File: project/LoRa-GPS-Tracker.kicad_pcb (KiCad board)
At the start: 2 copper layers, 38.9 x 40 mm, 58 parts, among them IC101 MCP73831-2-OT, IC102 MCP100-300D, IC103 FT230XS, IC104 NCP705MT30TCG, M101 SIM28ML, M102 RAK3172, Q101 BSS123, Q102 TP0610K, Q103 BSH205G2VL, SW102 ON/OFF, X101 DEBUG, X102 Conn_Coaxial, X103 BATTERY, X104 DEBUG

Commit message: - Fix wrong pinout for UART bootloader - Update documentation for bootloader
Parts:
- D101: value D_Zener -> SZMM5Z3V3T1G
- D103: value CLS6B-FKW -> STATUS
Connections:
- JP101 pad 1: /Rx_LOG -> /Rx_PROG
- JP101 pad 3: /Rx_PROG -> /Rx_LOG
- JP102 pad 1: /Tx_LOG -> /Tx_PROG
- JP102 pad 3: /Tx_PROG -> /Tx_LOG
- M102 pad 10: /Tx_PROG -> unconnected-(M102-SDA-Pad10)
- M102 pad 20: Net-(M102-PA9) -> /Rx_PROG
- M102 pad 25: unconnected-(M102-ADC4-Pad25) -> /Tx_PROG
- M102 pad 27: unconnected-(M102-PB12-Pad27) -> Net-(M102-PB12)
- M102 pad 9: /Rx_PROG -> unconnected-(M102-SCL-Pad9)
- R119 pad 1: Net-(M102-PA9) -> Net-(M102-PB12)
- X101 pad A8: unconnected-(X101-SBU1-PadA8) -> (no net)
- X101 pad B8: unconnected-(X101-SBU2-PadB8) -> (no net)
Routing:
- net Net-(M102-PB12): track 0.00 -> 44.2 mm, vias 0 -> 2
- net Net-(M102-PA9): track 43.4 -> 0.00 mm, vias 4 -> 0
- net /Tx_PROG: track 5.97 -> 12.9 mm
- net /Rx_PROG: track 9.58 -> 13.9 mm
- net /Tx_LOG: track 12.0 -> 8.75 mm
- net /Rx_LOG: track 15.7 -> 14.2 mm
- net /Rx: track 26.0 -> 25.1 mm

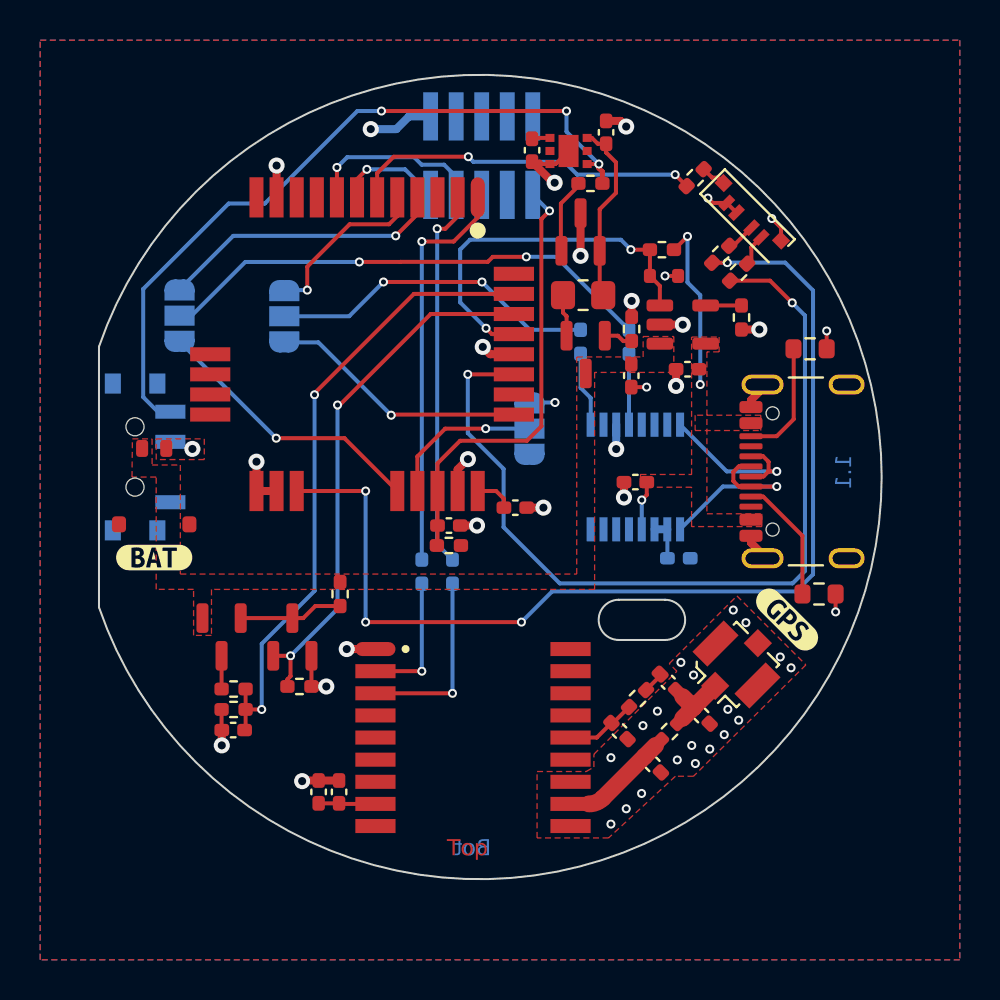
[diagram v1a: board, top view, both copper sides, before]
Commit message: Make it possible to power cycle the GPS module
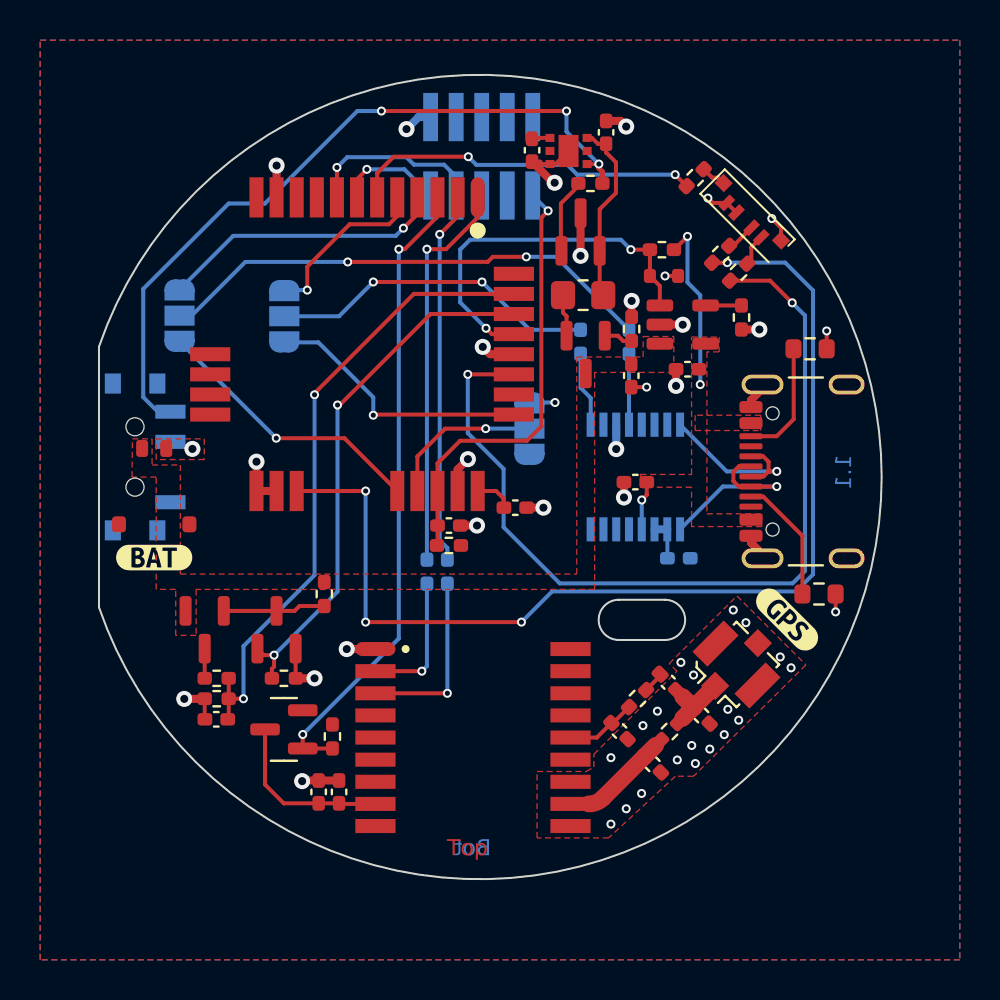
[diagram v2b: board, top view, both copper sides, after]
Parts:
- added Q104: TP0610K, Package_TO_SOT_SMD:SOT-23, F.Cu at (134.7, 118.7)
- added R122: 100k, Resistor_SMD:R_0402_1005Metric_Pad0.72x0.64mm_HandSolder, F.Cu at (137.2, 119.1)
- IC102: value MCP100-300D -> MCP100T-300I/TT
- moved kibuzzard-65A187C4 5.38 mm to (144.6, 94.2), turned to 180 degrees
- moved C103 0.99 mm to (131.4, 118.2)
- moved R105 0.99 mm to (131.4, 116.2)
- moved R106 0.99 mm to (131.4, 117.2)
- moved Q102 0.91 mm to (130.8, 113.8)
- moved R101 0.87 mm to (134.7, 116.2)
- moved Q101 0.86 mm to (134.4, 113.8)
- moved R104 0.79 mm to (136.8, 112.0)
- moved R102 0.25 mm to (141.9, 110.9)
- moved R103 0.25 mm to (142.9, 110.9)
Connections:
- C101 pad 1: +3V0 -> Net-(M101-VCC)
- C102 pad 1: +3V0 -> Net-(M101-VCC)
- M101 pad 8: +3V0 -> Net-(M101-VCC)
- M102 pad 3: unconnected-(M102-ADC5-Pad3) -> /GPS_E
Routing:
- net /GPS_E: track 0.00 -> 31.8 mm, vias 0 -> 2
- net Net-(M101-VCC): track 0.00 -> 8.63 mm
- net +3V0: track 11.4 -> 6.74 mm
- net /Tx_PROG: track 12.9 -> 13.5 mm

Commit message: Add I2C accelerometer
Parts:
- added C112: 100n, Capacitor_SMD:C_0402_1005Metric_Pad0.74x0.62mm_HandSolder, B.Cu at (134.2, 110.8)
- added IC105: LIS2DH, Package_LGA:LGA-14_2x2mm_P0.35mm_LayoutBorder3x4y, B.Cu at (132.3, 109.8)
- added R115: 3k3, Resistor_SMD:R_0402_1005Metric_Pad0.72x0.64mm_HandSolder, B.Cu at (131.3, 106.3)
- added R117: 3k3, Resistor_SMD:R_0402_1005Metric_Pad0.72x0.64mm_HandSolder, B.Cu at (133.2, 107.8)
- renumbered C104 to C103, C105 to C104, C106 to C105, C107 to C106, C108 to C107, C109 to C108, C110 to C109, C111 to C110, C112 to C111, C103 to C115, D103 to D102, Q104 to Q101, Q103 to Q102, Q101 to Q103, Q102 to Q104, R102 to R101, R103 to R102, R122 to R103, R107 to R104, R108 to R105, R109 to R106, R110 to R107, R111 to R108, R112 to R109, R113 to R110, R114 to R111, R115 to R112, R116 to R113, R117 to R114, R118 to R116, R101 to R118, R120 to R119, R119 to R120, R104 to R121, R121 to R122, R105 to R123, R106 to R124, SW102 to SW101
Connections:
- M102 pad 10: unconnected-(M102-SDA-Pad10) -> Net-(IC105-SDA/SDI)
- M102 pad 26: unconnected-(M102-ADC3-Pad26) -> /INT
- M102 pad 9: unconnected-(M102-SCL-Pad9) -> Net-(IC105-SCL/SPC)
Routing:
- net /INT: track 0.00 -> 20.4 mm, vias 0 -> 3
- net Net-(IC105-SCL/SPC): track 0.00 -> 18.7 mm, vias 0 -> 1
- net Net-(IC105-SDA/SDI): track 0.00 -> 18.1 mm, vias 0 -> 1
- net +3V0: track 6.74 -> 11.0 mm, vias 3 -> 7

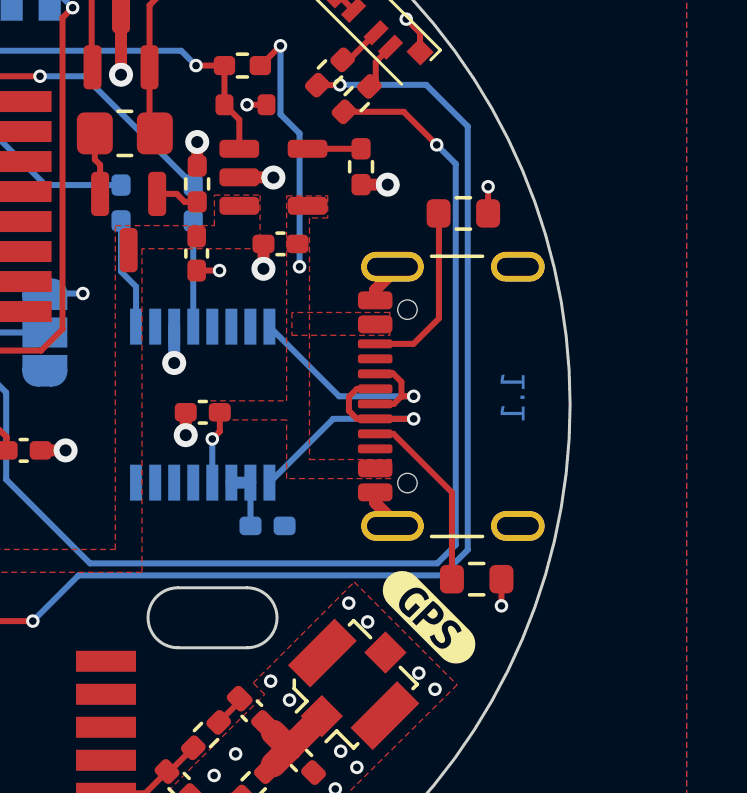
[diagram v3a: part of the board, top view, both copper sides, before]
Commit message: Fix wrong package for CC resistors
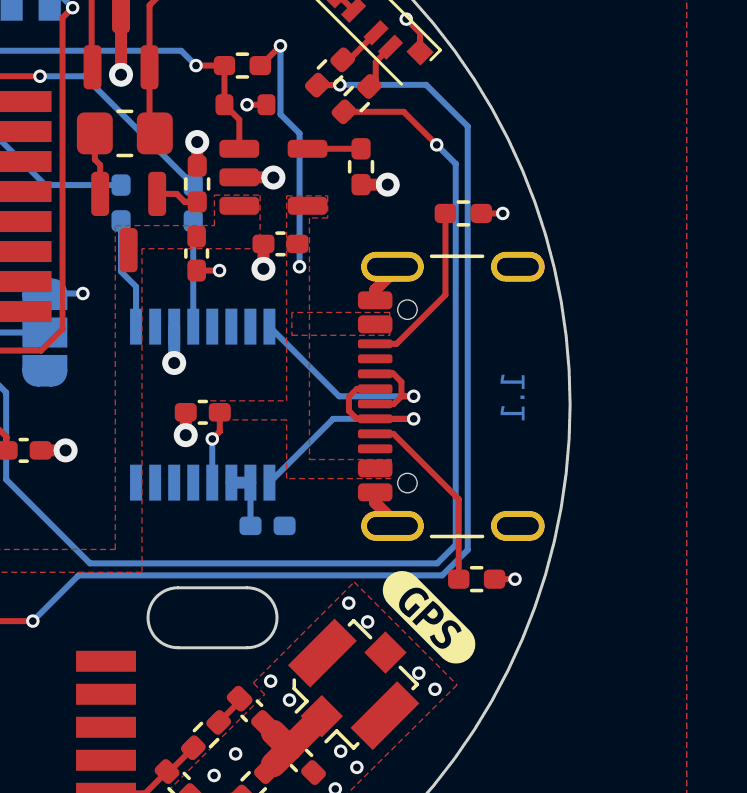
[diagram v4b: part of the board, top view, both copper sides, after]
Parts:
- Q101, Q104: value TP0610K -> BSS84
- R104, R105: footprint Resistor_SMD:R_0603_1608Metric -> Resistor_SMD:R_0402_1005Metric_Pad0.72x0.64mm_HandSolder

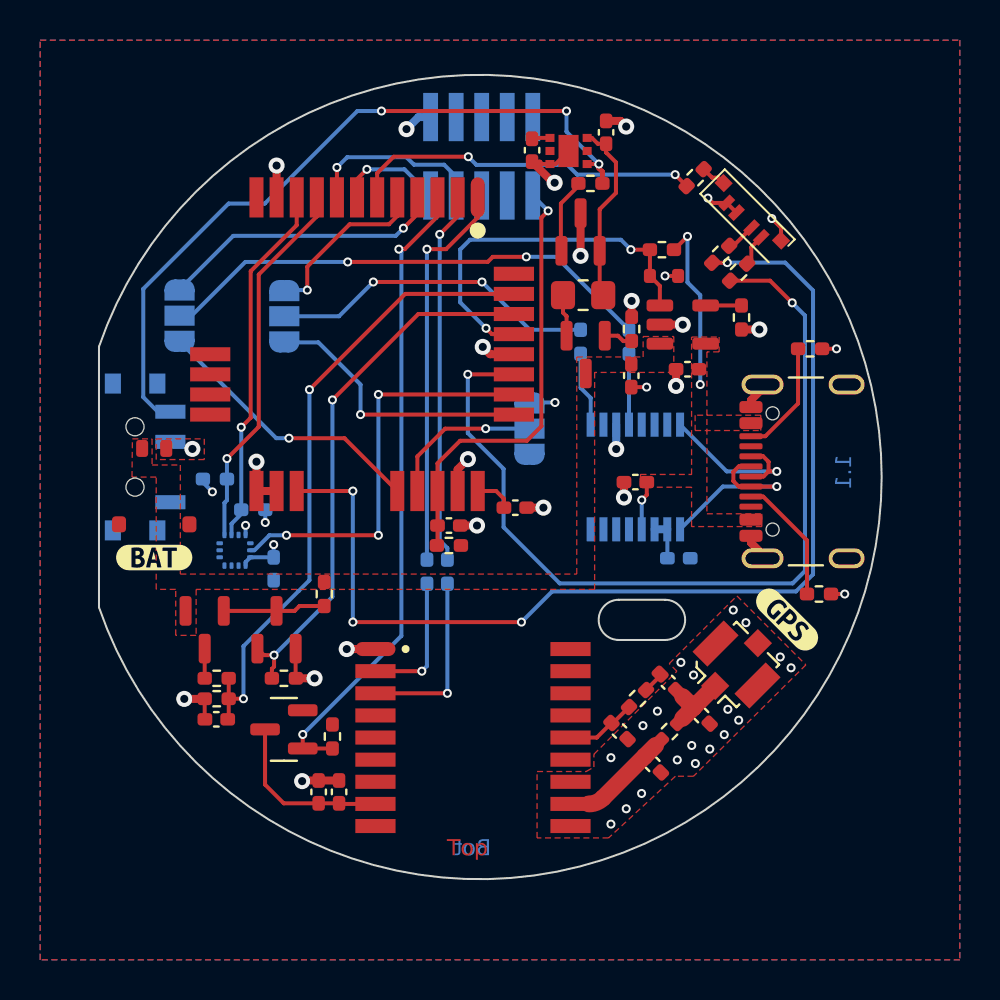
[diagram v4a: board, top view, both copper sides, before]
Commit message: Fix wrong footprint for status LED
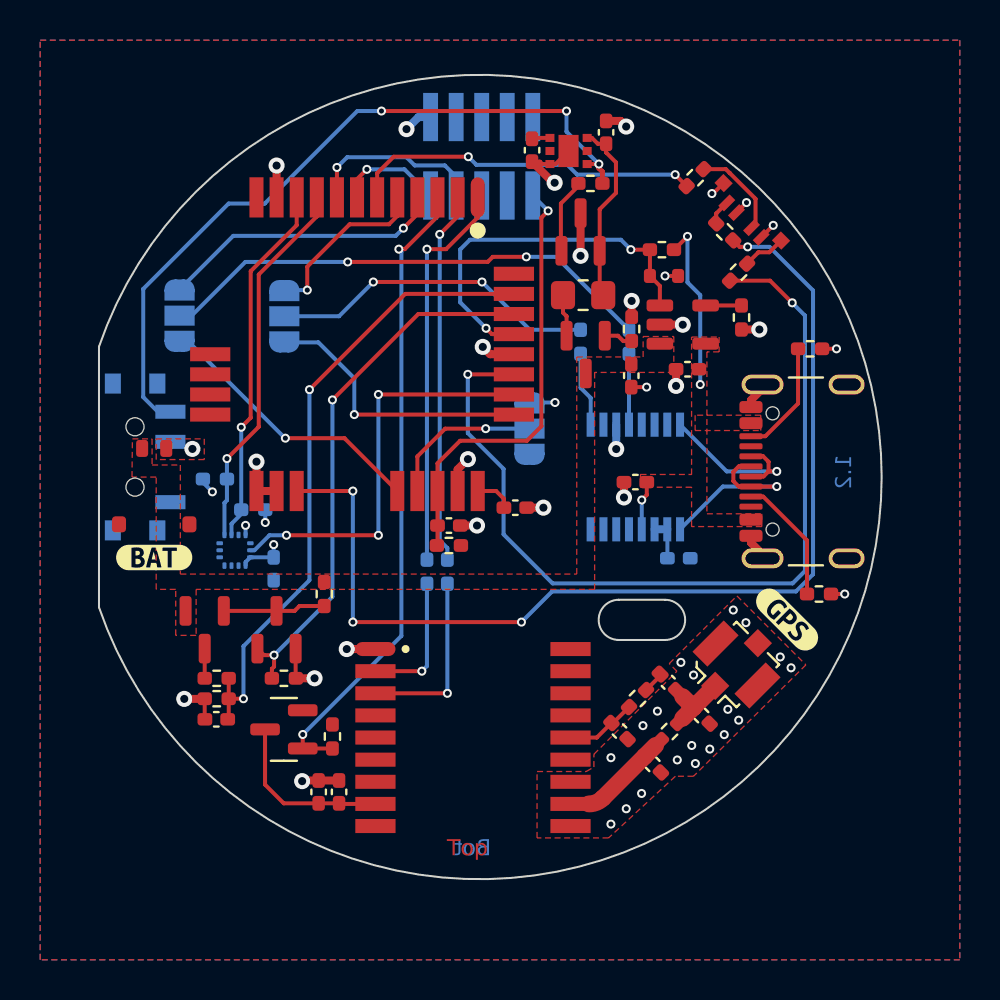
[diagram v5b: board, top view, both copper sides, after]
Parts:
- moved R119 1.13 mm to (156.7, 94.0), turned to 135 degrees
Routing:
- net Net-(D102-AR): track 1.28 -> 4.71 mm
- net GND: track 36.6 -> 36.0 mm, vias 44 -> 45
- net Net-(M102-PA8): track 52.9 -> 52.3 mm
- net Net-(D102-AB): track 1.60 -> 2.17 mm
